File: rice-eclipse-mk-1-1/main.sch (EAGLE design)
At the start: 75 parts, among them IC1 LMV321LICTRT, IC2 LMV321LICTRT, IC3 LMV321LICTRT, IC4 LMV321LICTRT, U1 LM1084ISX-5.0/NOPB, U2 THS4531IDRD8-M, U3 THS4531IDRD8-M, U4 THS4531IDRD8-M, U5 THS4531IDRD8-M, U6 1101M2S3CQE2, X1 2540-5

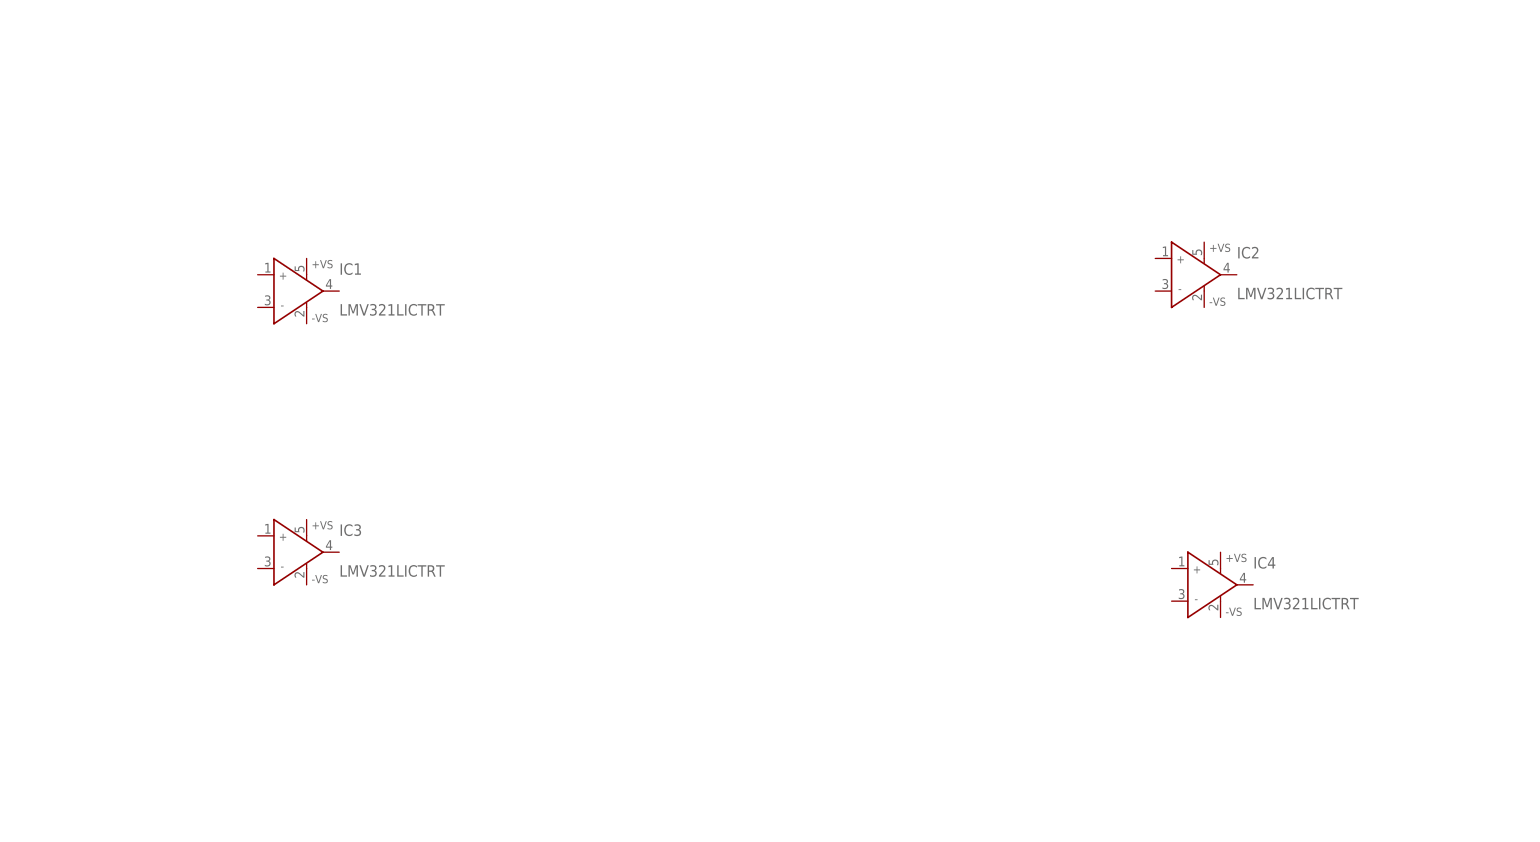
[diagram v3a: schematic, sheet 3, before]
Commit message: Added initial PT circuit guess and
added some routes for power.
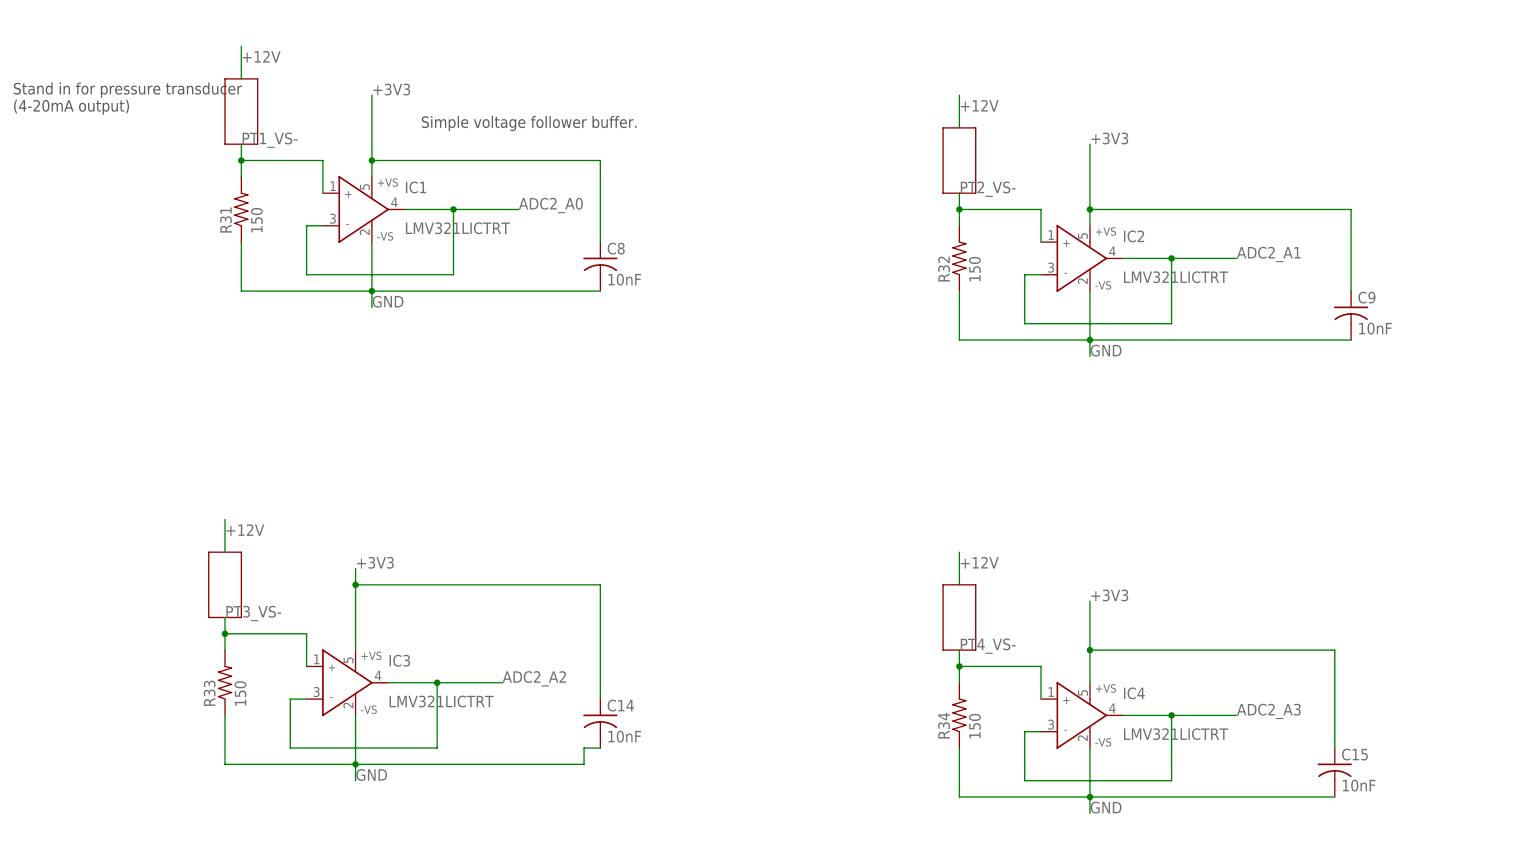
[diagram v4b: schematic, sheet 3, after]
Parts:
- added C14, C15, C8, C9: 10nF, rcl:C-USC0603
- added R31, R32, R33, R34: 150, rcl:R-US_R0603
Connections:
- new net PT1_VS-: IC1.IN+, R31.2, X2-5.SK
- new net PT2_VS-: IC2.IN+, R32.2, X2-3.SK
- new net PT3_VS-: IC3.IN+, R33.2, X2-1.SK
- new net PT4_VS-: IC4.IN+, R34.2, X3-5.SK
- net +12V: now also X2-2.SK, X2-4.SK, X2-6.SK, X3-6.SK
- net +3V3: now also C14.1, C15.1, C8.1, C9.1, IC1.+VS, IC2.+VS, IC3.+VS, IC4.+VS
- net ADC2_A0: now also IC1.IN-, IC1.OUT; no longer X2-6.SK
- net ADC2_A1: now also IC2.IN-, IC2.OUT; no longer X2-5.SK
- net ADC2_A2: now also IC3.IN-, IC3.OUT; no longer X2-4.SK
- net ADC2_A3: now also IC4.IN-, IC4.OUT; no longer X2-3.SK
- net ADC2_A4: now also X3-4.SK
- net ADC2_A5: now also X3-3.SK
- net ADC2_A6: now also X3-2.SK
- net ADC2_A7: now also X3-1.SK
- net GND: now also C14.2, C15.2, C8.2, C9.2, IC1.-VS, IC2.-VS, IC3.-VS, IC4.-VS, R31.1, R32.1, R33.1, R34.1
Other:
- note added: "Simple voltage follower buffer."
- note added: "Stand in for pressure transducer (4-20mA output)"
- moved on the sheet: IC1, IC2, IC3, IC4

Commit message: Made a bunch of stuff.
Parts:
- added C16: 0.1UF, rcl:CPOL-USE2.5-5
- added C17: 0.33UF, rcl:CPOL-USE2.5-5
- added C18: 10nF, rcl:C-USC0603
- added C19, C20: (no value), rcl:C-US025-025X050
- added IC5: UA78M, texas-extra:UA78M
- added IC6: LMV321LICTRT, st-microelectronics-extra:LMV321LICTRT
- added JP1, JP2, JP3: (no value), pinhead:PINHD-1X2
- added LED4: (no value), led:LED5MM
- added R35: 470, resistor:R-US_R0603
- added R36, R37, R38, R39, R40, R41: ?, rcl:R-US_0204/7
- added U7: 1101M2S3CQE2, SLIDE_SW:1101M2S3CQE2
- C4, C5: device rcl:C-USC0603 -> rcl:CPOL-USE2.5-5
- C6, C7: device rcl:C-US025-050X050 -> rcl:CPOL-USE2.5-5
- R31: value 150 -> 10
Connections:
- new net +3V3_ADC: ADC1.VDD, ADC1.VREF, ADC2.VDD, ADC2.VREF, ADC3.VDD, ADC3.VREF, C1.1, C2.1, C3.1, JP1.2, R25.2, R29.2, R30.2
- new net +3V3_LC: C10.1, C11.1, C12.1, C13.1, JP3.2, R12.2, R17.2, R21.2, R9.2, U2.VS+, U3.VS+, U4.VS+, U5.VS+
- new net +3V3_PT: C14.1, C15.1, C18.1, C8.1, C9.1, IC1.+VS, IC2.+VS, IC3.+VS, IC4.+VS, IC6.+VS, JP2.2, R38.1
- new net +5V_RPI: X1-2.KL
- new net N$10: IC1.IN-, R36.1, R37.2
- new net N$11: C19.1, R40.2, R41.1
- new net N$12: IC1.IN+, R38.2, R39.1
- new net N$25: C20.1, IC6.IN+, R40.1
- new net N$4: C16.+, IC5.VO, U7.P
- new net N$9: LED4.C, R35.1
- new net PT1_PREC: IC1.OUT, R37.1, R41.2
- net +10V: now also C6.+, R35.2, U1.VIN, U7.O
- net +12V: now also C17.+, IC5.VI; no longer C5.1, C6.1, REG1.VIN, U1.VIN
- net +3V3: now also C4.+, JP1.1, JP2.1, JP3.1; no longer ADC1.VDD, ADC1.VREF, ADC2.VDD, ADC2.VREF, ADC3.VDD, ADC3.VREF, C1.1, C10.1, C11.1, C12.1, C13.1, C14.1, C15.1, C2.1, C3.1, C4.1, C8.1, C9.1, IC1.+VS, IC2.+VS, IC3.+VS, IC4.+VS, R12.2, R17.2, R21.2, R25.2, R29.2, R30.2, R9.2, U2.VS+, U3.VS+, U4.VS+, U5.VS+
- net +5V: now also C5.+, C7.+, REG1.VIN; no longer C7.1, X1-2.KL
- net ADC2_A0: now also IC6.IN-, IC6.OUT; no longer IC1.IN-, IC1.OUT
- net GND: now also C16.-, C17.-, C18.2, C19.2, C20.2, C4.-, C5.-, C6.-, C7.-, IC5.GND, IC6.-VS, LED4.A, R39.2; no longer C4.2, C5.2, C6.2, C7.2
- net PT1_VS-: now also R36.2; no longer IC1.IN+
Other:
- note added: "DO NOT CONNECT"
- note added: "TODO: Design 2nd order LPF"
- note removed: "Simple voltage follower buffer."
- moved on the sheet: C8, IC1, REG1
